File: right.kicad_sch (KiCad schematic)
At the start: 134 parts, among them J2 Pointing stick, J3 PWRSWITCH, J5 Conn_01x01_Female, SW10 SW_Push, SW11 SW_Push, SW12 SW_Push, SW13 SW_Push, SW14 SW_Push, SW15 SW_Push, SW23 SW_Push, SW24 SW_Push, SW25 SW_Push, SW26 SW_Push, SW27 SW_Push, SW28 SW_Push, SW29 SW_Push, SW30 SW_Push, SW38 SW_Push, SW39 SW_Push, SW40 SW_Push, SW41 SW_Push, SW42 SW_Push, SW43 SW_Push, SW44 SW_Push, SW45 SW_Push, SW54 SW_Push, SW55 SW_Push, SW56 SW_Push, SW57 SW_Push, SW58 SW_Push, SW59 SW_Push, SW60 SW_Push, SW69 SW_Push, SW70 SW_Push, SW71 SW_Push, SW72 SW_Push, SW73 SW_Push, SW74 SW_Push, SW75 SW_Push, SW8 SW_Push, SW83 SW_Push, SW84 SW_Push, SW85 SW_Push, SW86 SW_Push, SW87 SW_Push, SW88 SW_Push, SW89 SW_Push, SW9 SW_Push, SW90 SW_Push, U2 Elite-C

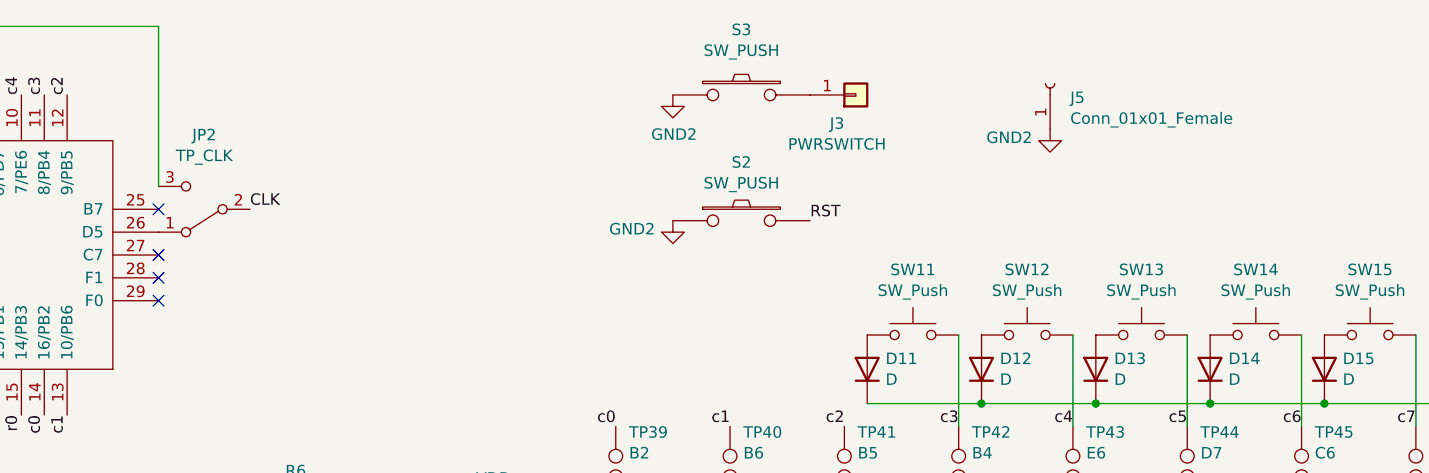
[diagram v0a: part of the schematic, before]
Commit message: make changes for higher mcu position/potential bat
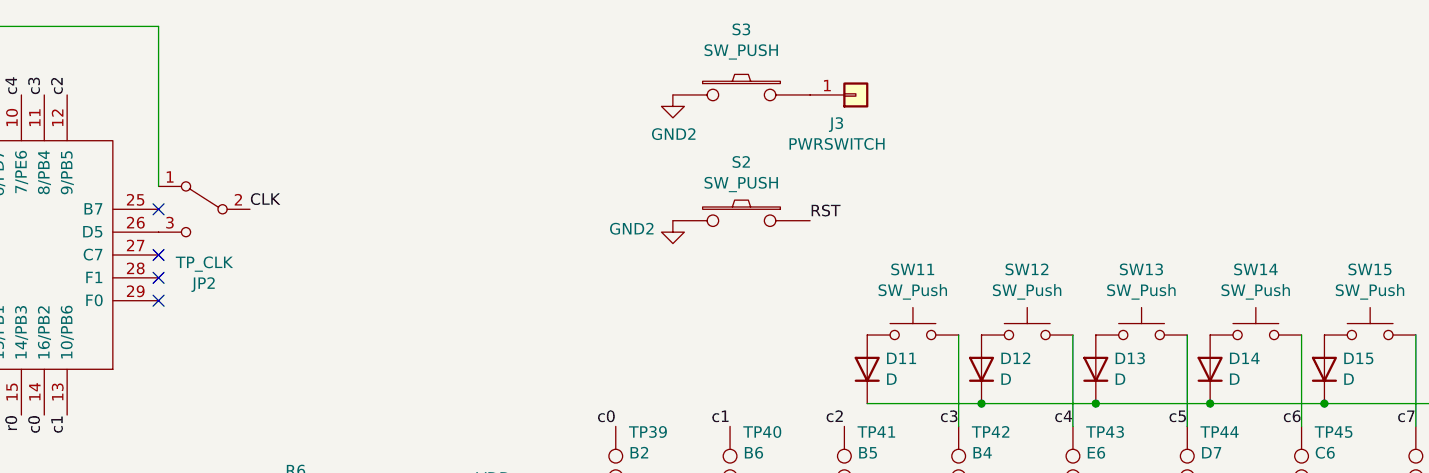
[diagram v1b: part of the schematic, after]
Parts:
- removed J5: Conn_01x01_Female, TestPoint:TestPoint_Pad_1.0x1.0mm, symbol Connector:Conn_01x01_Female
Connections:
- net GND2: now also S2.2; no longer S2.1
- net RST: now also S2.1; no longer S2.2
- net at U2.1 (TX0/PD3): now also JP2.1 (A); no longer JP2.3 (C)
- net at U2.26 (D5): now also JP2.3 (C); no longer JP2.1 (A)
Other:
- moved on the sheet: JP2
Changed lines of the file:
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@@
     (pin "1")
   )
-  (symbol (lib_id "kbd:SW_PUSH") (at 127 34.29 0) (unit 1)
+  (symbol (lib_id "kbd:SW_PUSH") (at 127 34.29 0) (mirror y) (unit 1)
     (in_bom yes) (on_board yes)
     (property "Reference" "S2" (id 0) (at 127 27.813 0))
@@
     (pin "1")
   )
-  (symbol (lib_id "Connector:TestPoint") (at 176.53 66.04 0)
+  (symbol (lib_id "Connector:TestPoint") (at 176.53 66.04 0) (unit 1)
     (in_bom yes) (on_board yes)
     (property "Reference" "TP52" (id 0) (at 178.0032 63.0428 0)
@@
     (pin "1")
   )
-  (symbol (lib_id "Connector:TestPoint") (at 163.83 66.04 0)
+  (symbol (lib_id "Connector:TestPoint") (at 163.83 66.04 0) (unit 1)
     (in_bom yes) (on_board yes)
     (property "Reference" "TP51" (id 0) (at 165.3032 63.0428 0)
@@
     (pin "1")
   )
-  (symbol (lib_id "Connector:TestPoint") (at 151.13 66.04 0)
+  (symbol (lib_id "Connector:TestPoint") (at 151.13 66.04 0) (unit 1)
     (in_bom yes) (on_board yes)
     (property "Reference" "TP50" (id 0) (at 152.6032 63.0428 0)
@@
     (pin "1")
   )
-  (symbol (lib_id "Connector:TestPoint") (at 138.43 66.04 0)
+  (symbol (lib_id "Connector:TestPoint") (at 138.43 66.04 0) (unit 1)
     (in_bom yes) (on_board yes)
     (property "Reference" "TP49" (id 0) (at 139.9032 63.0428 0)
@@
     (pin "1")
   )
-  (symbol (lib_id "Connector:TestPoint") (at 125.73 66.04 0)
+  (symbol (lib_id "Connector:TestPoint") (at 125.73 66.04 0) (unit 1)
     (in_bom yes) (on_board yes)
     (property "Reference" "TP48" (id 0) (at 127.2032 63.0428 0)
@@
     (pin "1")
   )
-  (symbol (lib_id "Connector:TestPoint") (at 189.23 66.04 0)
+  (symbol (lib_id "Connector:TestPoint") (at 189.23 66.04 0) (unit 1)
     (in_bom yes) (on_board yes)
     (property "Reference" "TP53" (id 0) (at 190.7032 63.0428 0)
@@
     (pin "1")
   )
-  (symbol (lib_id "Connector:TestPoint") (at 138.43 57.15 180)
+  (symbol (lib_id "Connector:TestPoint") (at 138.43 57.15 180) (unit 1)
     (in_bom yes) (on_board yes)
     (property "Reference" "TP41" (id 0) (at 139.9032 57.8104 0)
@@
     (pin "1")
   )
-  (symbol (lib_id "Connector:TestPoint") (at 151.13 57.15 180)
+  (symbol (lib_id "Connector:TestPoint") (at 151.13 57.15 180) (unit 1)
     (in_bom yes) (on_board yes)
     (property "Reference" "TP42" (id 0) (at 152.6032 57.8104 0)
@@
     (pin "1")
   )
-  (symbol (lib_id "Connector:TestPoint") (at 163.83 57.15 180)
+  (symbol (lib_id "Connector:TestPoint") (at 163.83 57.15 180) (unit 1)
     (in_bom yes) (on_board yes)
     (property "Reference" "TP43" (id 0) (at 165.3032 57.8104 0)
@@
     (pin "1")
   )
-  (symbol (lib_id "Connector:TestPoint") (at 176.53 57.15 180)
+  (symbol (lib_id "Connector:TestPoint") (at 176.53 57.15 180) (unit 1)
     (in_bom yes) (on_board yes)
     (property "Reference" "TP44" (id 0) (at 178.0032 57.8104 0)
@@
     (pin "1")
   )
-  (symbol (lib_id "Connector:TestPoint") (at 189.23 57.15 180)
+  (symbol (lib_id "Connector:TestPoint") (at 189.23 57.15 180) (unit 1)
     (in_bom yes) (on_board yes)
     (property "Reference" "TP45" (id 0) (at 190.7032 57.8104 0)
@@
     (pin "1")
   )
-  (symbol (lib_id "Connector:TestPoint") (at 113.03 57.15 180)
+  (symbol (lib_id "Connector:TestPoint") (at 113.03 57.15 180) (unit 1)
     (in_bom yes) (on_board yes)
     (property "Reference" "TP39" (id 0) (at 114.5032 57.8104 0)
@@
     (pin "1")
   )
-  (symbol (lib_id "Connector:TestPoint") (at 125.73 57.15 180)
+  (symbol (lib_id "Connector:TestPoint") (at 125.73 57.15 180) (unit 1)
     (in_bom yes) (on_board yes)
     (property "Reference" "TP40" (id 0) (at 127.2032 57.8104 0)
@@
     (pin "1")
   )
-  (symbol (lib_id "Connector:TestPoint") (at 113.03 66.04 0)
+  (symbol (lib_id "Connector:TestPoint") (at 113.03 66.04 0) (unit 1)
     (in_bom yes) (on_board yes)
     (property "Reference" "TP47" (id 0) (at 114.5032 63.0428 0)
@@
     (pin "1")
   )
-  (symbol (lib_id "Connector:TestPoint") (at 201.93 66.04 0)
+  (symbol (lib_id "Connector:TestPoint") (at 201.93 66.04 0) (unit 1)
     (in_bom yes) (on_board yes)
     (property "Reference" "TP54" (id 0) (at 203.4032 63.0428 0)
@@
     (pin "1")
   )
-  (symbol (lib_id "Connector:TestPoint") (at 201.93 57.15 180)
+  (symbol (lib_id "Connector:TestPoint") (at 201.93 57.15 180) (unit 1)
     (in_bom yes) (on_board yes)
     (property "Reference" "TP46" (id 0) (at 203.4032 57.8104 0)
@@
     (pin "1")
   )
-  (symbol (lib_id "keebio:HRO-TYPE-C-31-M-12") (at 24.13 93.98 0)
+  (symbol (lib_id "keebio:HRO-TYPE-C-31-M-12") (at 24.13 93.98 0) (unit 1)
     (in_bom yes) (on_board yes)
     (property "Reference" "USB2" (id 0) (at 20.32 77.47 0)
@@
     (pin "1")
   )
-  (symbol (lib_id "Connector:Conn_01x01_Female") (at 161.29 19.05 90) (unit 1)
-    (in_bom yes) (on_board yes)
-    (property "Reference" "J5" (id 0) (at 163.5252 20.6248 90)
-      (effects (font (size 1.27 1.27)) (justify right))
-    )
-    (property "Value" "Conn_01x01_Female" (id 1) (at 163.5252 22.9362 90)
-      (effects (font (size 1.27 1.27)) (justify right))
-    )
-    (property "Footprint" "TestPoint:TestPoint_Pad_1.0x1.0mm" (id 2) (at 161.29 19.05 0)
-      (effects (font (size 1.27 1.27)) hide)
-    )
-    (property "Datasheet" "~" (id 3) (at 161.29 19.05 0)
-      (effects (font (size 1.27 1.27)) hide)
-    )
-    (pin "1")
-  )
-  (symbol (lib_id "power:GND2") (at 161.29 24.13 0) (unit 1)
-    (in_bom yes) (on_board yes)
-    (property "Reference" "#PWR0118" (id 0) (at 161.29 30.48 0)
-      (effects (font (size 1.27 1.27)) hide)
-    )
-    (property "Value" "GND2" (id 1) (at 159.3088 25.0698 0)
-      (effects (font (size 1.27 1.27)) (justify right))
-    )
-    (property "Footprint" "" (id 2) (at 161.29 24.13 0)
-      (effects (font (size 1.27 1.27)) hide)
-    )
-    (property "Datasheet" "" (id 3) (at 161.29 24.13 0)
-      (effects (font (size 1.27 1.27)) hide)
-    )
-    (pin "1")
-  )
-  (symbol (lib_id "Connector:TestPoint") (at 278.13 66.04 0) (mirror y)
+  (symbol (lib_id "Connector:TestPoint") (at 278.13 66.04 0) (mirror y) (unit 1)
     (in_bom yes) (on_board yes)
     (property "Reference" "TP19" (id 0) (at 279.6032 63.0428 0)
@@
     (pin "1")
   )
-  (symbol (lib_id "Connector:TestPoint") (at 214.63 57.15 180)
+  (symbol (lib_id "Connector:TestPoint") (at 214.63 57.15 180) (unit 1)
     (in_bom yes) (on_board yes)
     (property "Reference" "TP18" (id 0) (at 216.1032 57.8104 0)
@@
     (pin "1")
   )
-  (symbol (lib_id "Connector:TestPoint") (at 227.33 57.15 180)
+  (symbol (lib_id "Connector:TestPoint") (at 227.33 57.15 180) (unit 1)
     (in_bom yes) (on_board yes)
     (property "Reference" "TP17" (id 0) (at 228.8032 57.8104 0)
@@
     (pin "1")
   )
-  (symbol (lib_id "Connector:TestPoint") (at 240.03 57.15 180)
+  (symbol (lib_id "Connector:TestPoint") (at 240.03 57.15 180) (unit 1)
     (in_bom yes) (on_board yes)
     (property "Reference" "TP16" (id 0) (at 241.5032 57.8104 0)
@@
     (pin "1")
   )
-  (symbol (lib_id "Connector:TestPoint") (at 252.73 57.15 180)
+  (symbol (lib_id "Connector:TestPoint") (at 252.73 57.15 180) (unit 1)
     (in_bom yes) (on_board yes)
     (property "Reference" "TP15" (id 0) (at 254.2032 57.8104 0)
@@
     (pin "1")
   )
-  (symbol (lib_id "Connector:TestPoint") (at 265.43 57.15 180)
+  (symbol (lib_id "Connector:TestPoint") (at 265.43 57.15 180) (unit 1)
     (in_bom yes) (on_board yes)
     (property "Reference" "TP14" (id 0) (at 266.9032 57.8104 0)
@@
     (pin "1")
   )
-  (symbol (lib_id "Connector:TestPoint") (at 278.13 57.15 180)
+  (symbol (lib_id "Connector:TestPoint") (at 278.13 57.15 180) (unit 1)
     (in_bom yes) (on_board yes)
     (property "Reference" "TP13" (id 0) (at 279.6032 57.8104 0)
@@
     (pin "1")
   )
-  (symbol (lib_id "Connector:TestPoint") (at 214.63 66.04 0) (mirror y)
+  (symbol (lib_id "Connector:TestPoint") (at 214.63 66.04 0) (mirror y) (unit 1)
     (in_bom yes) (on_board yes)
     (property "Reference" "TP20" (id 0) (at 216.1032 63.0428 0)
@@
     (pin "1")
   )
-  (symbol (lib_id "Connector:TestPoint") (at 227.33 66.04 0) (mirror y)
+  (symbol (lib_id "Connector:TestPoint") (at 227.33 66.04 0) (mirror y) (unit 1)
     (in_bom yes) (on_board yes)
     (property "Reference" "TP21" (id 0) (at 228.8032 63.0428 0)
@@
     (pin "1")
   )
-  (symbol (lib_id "Connector:TestPoint") (at 240.03 66.04 0) (mirror y)
+  (symbol (lib_id "Connector:TestPoint") (at 240.03 66.04 0) (mirror y) (unit 1)
     (in_bom yes) (on_board yes)
     (property "Reference" "TP22" (id 0) (at 241.5032 63.0428 0)
@@
     (pin "1")
   )
-  (symbol (lib_id "Connector:TestPoint") (at 252.73 66.04 0) (mirror y)
+  (symbol (lib_id "Connector:TestPoint") (at 252.73 66.04 0) (mirror y) (unit 1)
     (in_bom yes) (on_board yes)
     (property "Reference" "TP23" (id 0) (at 254.2032 63.0428 0)
@@
     (pin "1")
   )
-  (symbol (lib_id "Connector:TestPoint") (at 265.43 66.04 0) (mirror y)
+  (symbol (lib_id "Connector:TestPoint") (at 265.43 66.04 0) (mirror y) (unit 1)
     (in_bom yes) (on_board yes)
     (property "Reference" "TP24" (id 0) (at 266.9032 63.0428 0)
@@
     (pin "2")
   )
-  (symbol (lib_id "Switch:SW_SPDT") (at 67.31 33.02 180) (unit 1)
-    (in_bom yes) (on_board yes)
-    (property "Reference" "JP2" (id 0) (at 67.31 24.765 0))
-    (property "Value" "TP_CLK" (id 1) (at 67.31 27.0764 0))
+  (symbol (lib_id "Switch:SW_SPDT") (at 67.31 33.02 0) (mirror y) (unit 1)
+    (in_bom yes) (on_board yes)
+    (property "Reference" "JP2" (id 0) (at 67.31 41.275 0))
+    (property "Value" "TP_CLK" (id 1) (at 67.31 38.9636 0))
     (property "Footprint" "libmodulo:SolderJumper-3_P1.3mm_Open_RoundedPad1.0x1.5mm_NumberLabels" (id 2) (at 67.31 33.02 0)
       (effects (font (size 1.27 1.27)) hide)
